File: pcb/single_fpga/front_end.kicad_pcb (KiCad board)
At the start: 4 copper layers, 120 x 120 mm, 71 parts, among them CON1 AXK680337YG, CON2 AXK680337YG, CON3 AXK680337YG, CON4 AXK680337YG, J1 Main Power Input, J2 AXK5S80337YG, J3 HR911130A, J4 JTAG_HDR_2x7_2mm, U1 TLV62569DBV, U3 DP83867IRRGZ, U4 TLV75525PDBV, U5 TLV75510PDRV, U6 TLV62569DBV, Y1 25MHz

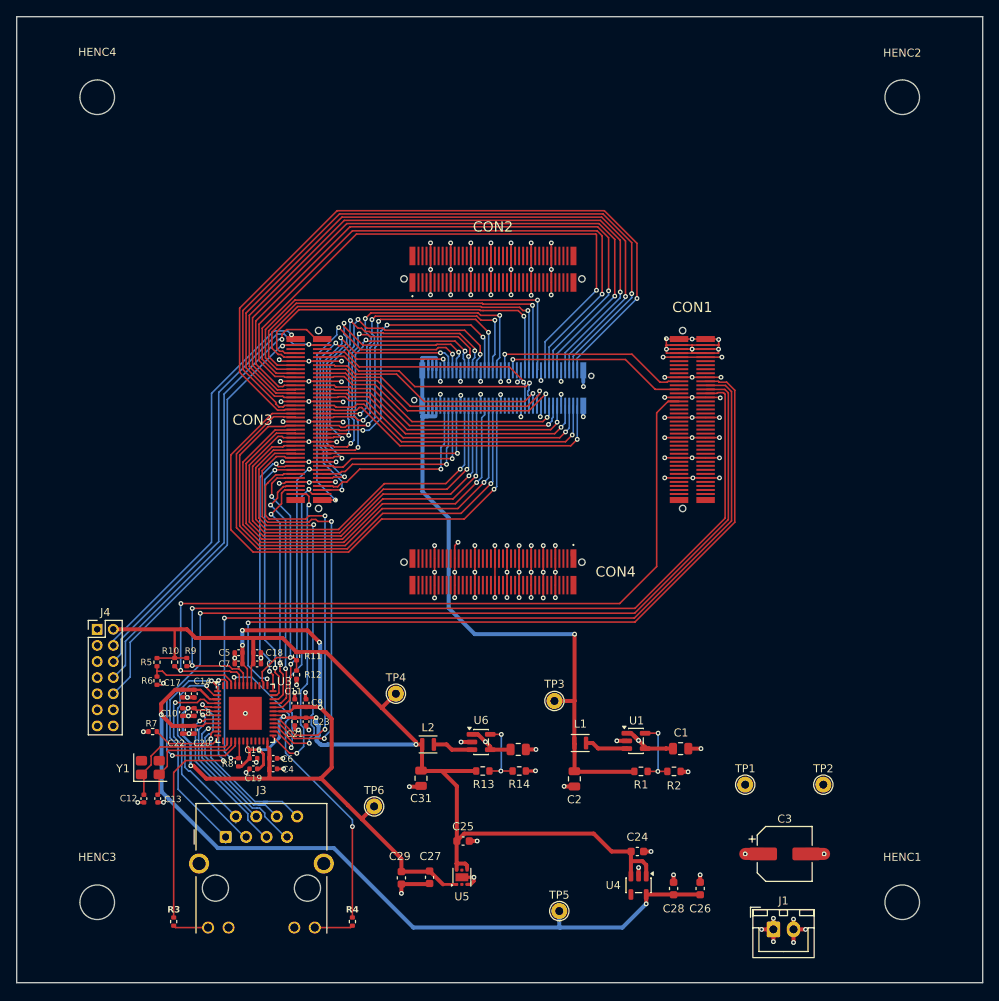
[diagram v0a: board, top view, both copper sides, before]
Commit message: Fixed thermal pad. Moved RGMII lines to be in the same bank.
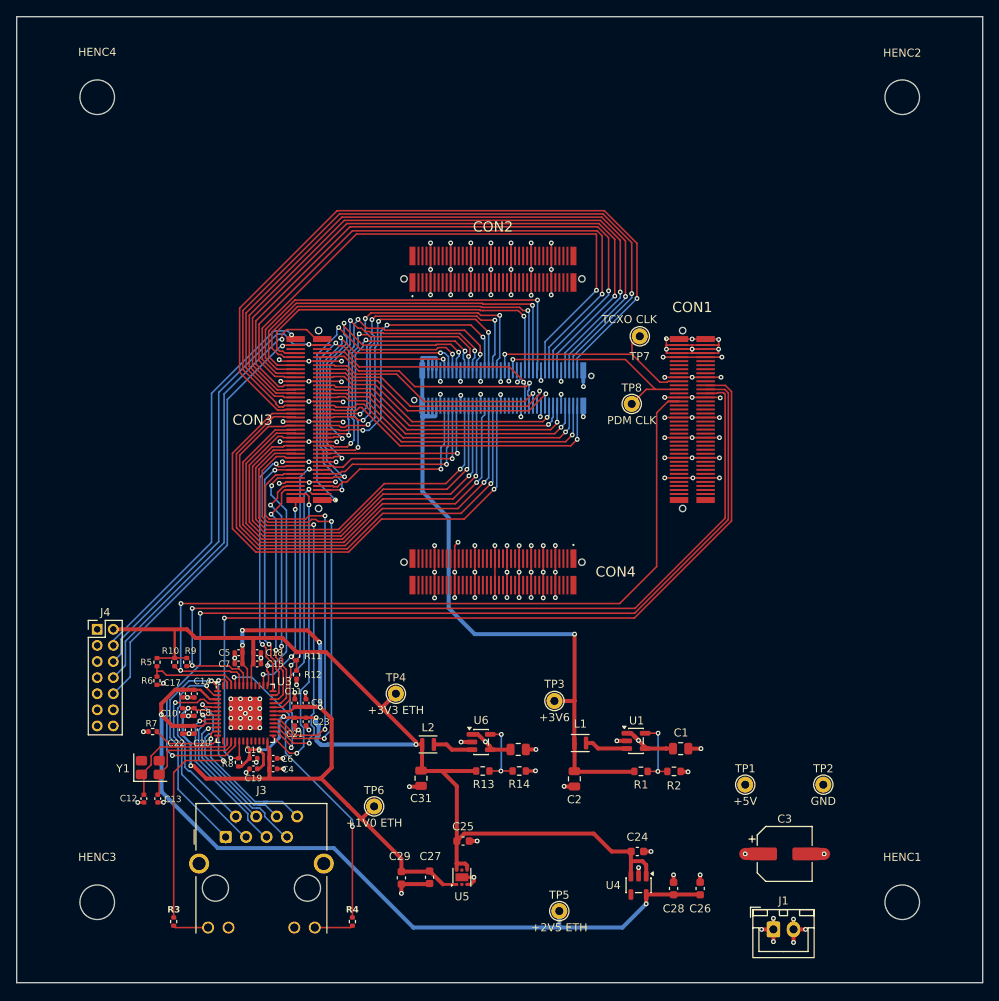
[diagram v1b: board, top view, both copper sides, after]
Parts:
- added TP7: TCXO CLK, TestPoint:TestPoint_THTPad_D2.0mm_Drill1.0mm, F.Cu at (117.4, 79.7)
- added TP8: PDM CLK, TestPoint:TestPoint_THTPad_D2.0mm_Drill1.0mm, F.Cu at (116.4, 88.1)
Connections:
- CON1 pad 22: RGMII_TX_CTL -> unconnected-(CON1-B13_L1_P-Pad22)
- CON3 pad 12: RGMII_RX_CTL -> RGMII_TX_CTL
- CON3 pad 2: unconnected-(CON3-B15_IO25-Pad2) -> RGMII_RX_CTL
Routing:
- net RGMII_TX_CTL: track 95.3 -> 30.7 mm
- net RGMII_RX_CTL: track 34.0 -> 27.7 mm, vias 2 -> 3
- net PDM_CLK: track 23.5 -> 27.2 mm
- net TCXO_CLK: track 25.1 -> 27.8 mm
- net GND: vias 143 -> 159

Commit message: Added more GND test points.
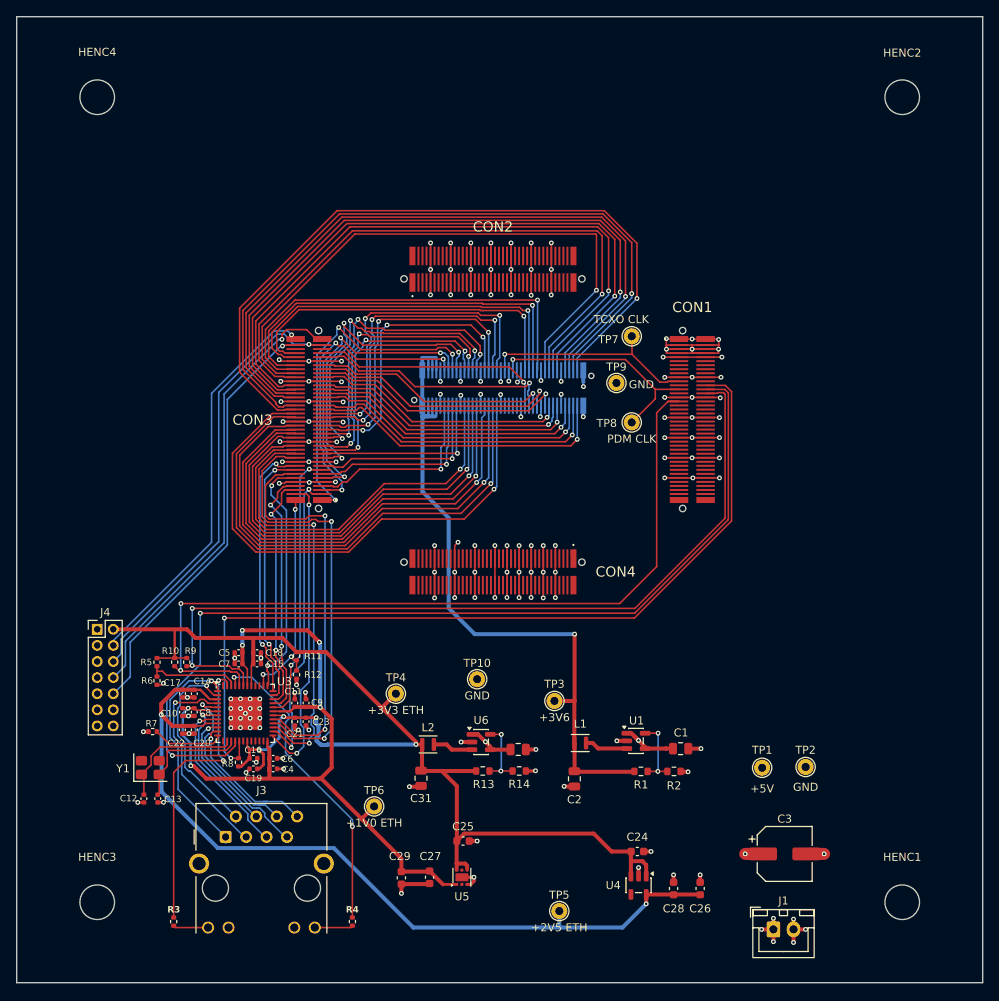
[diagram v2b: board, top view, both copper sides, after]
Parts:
- added TP10: GND, TestPoint:TestPoint_THTPad_D2.0mm_Drill1.0mm, F.Cu at (97.2, 122.3)
- added TP9: GND, TestPoint:TestPoint_THTPad_D2.0mm_Drill1.0mm, F.Cu at (114.5, 85.5)
- moved TP2 3.11 mm to (138.0, 133.2)
- moved TP1 2.97 mm to (132.6, 133.3)
- moved TP8 2.30 mm to (116.4, 90.4)
- moved TP7 1.00 mm to (116.4, 79.7)
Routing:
- net PDM_CLK: track 27.2 -> 28.8 mm

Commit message: Added RGB status LED.
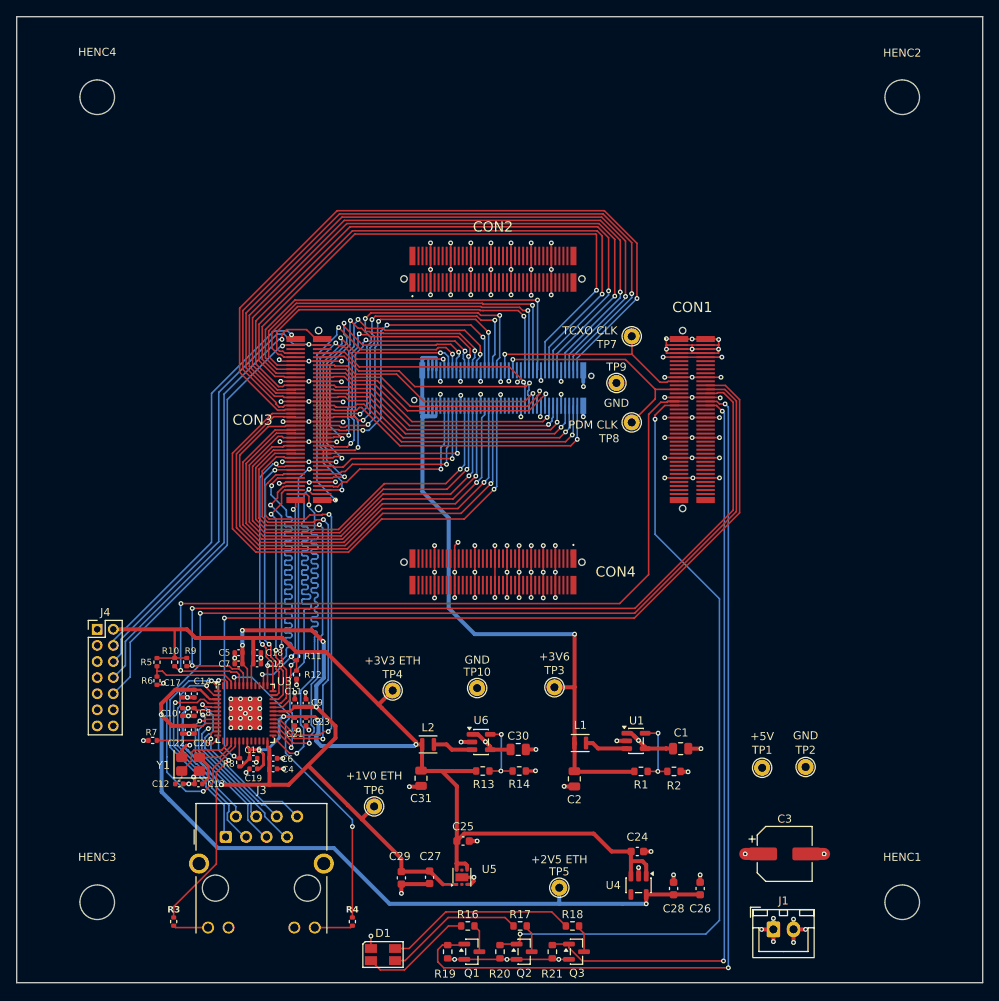
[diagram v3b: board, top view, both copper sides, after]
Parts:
- added D1: ASMB-MTB0-0A3A2, LED_SMD:LED_Avago_PLCC4_3.2x2.8mm_CW, F.Cu at (85.5, 156.5)
- added Q1: 2N7002, Package_TO_SOT_SMD:SOT-23, F.Cu at (96.5, 156.2)
- added Q2: 2N7002, Package_TO_SOT_SMD:SOT-23, F.Cu at (103.0, 156.2)
- added Q3: 2N7002, Package_TO_SOT_SMD:SOT-23, F.Cu at (109.5, 156.2)
- added R16: 620, PCM_SparkFun-Resistor:R_0603_1608Metric, F.Cu at (96.0, 152.9)
- added R17: 390, PCM_SparkFun-Resistor:R_0603_1608Metric, F.Cu at (102.5, 152.9)
- added R18: 390, PCM_SparkFun-Resistor:R_0603_1608Metric, F.Cu at (109.0, 152.9)
- added R19: 100k, PCM_SparkFun-Resistor:R_0603_1608Metric, F.Cu at (93.5, 156.2)
- added R20: 100k, PCM_SparkFun-Resistor:R_0603_1608Metric, F.Cu at (100.0, 156.2)
- added R21: 100k, PCM_SparkFun-Resistor:R_0603_1608Metric, F.Cu at (106.5, 156.2)
- Y1: value 25MHz -> 25MHz ±50 ppm max parallel resonant
- moved C13 5.38 mm to (62.6, 135.3), turned to 180 degrees
- moved Y1 5.02 mm to (61.6, 132.8)
- moved C12 4.74 mm to (60.2, 135.3), turned to 0 degrees
- moved TP5 2.90 mm to (107.4, 148.2)
- moved TP3 1.70 mm to (106.8, 123.3)
- moved TP10 1.10 mm to (97.2, 123.4)
- moved R7 1.10 mm to (56.9, 129.9)
- moved TP4 0.57 mm to (86.7, 123.7)
- moved R8 0.15 mm to (67.7, 132.6)
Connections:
- CON1 pad 32: unconnected-(CON1-B13_L6_P-Pad32) -> LED_R
- CON1 pad 33: unconnected-(CON1-B13_L3_N-Pad33) -> LED_G
- CON1 pad 34: unconnected-(CON1-B13_L6_N-Pad34) -> LED_B
- Y1 pad 2: Net-(U3-XI) -> GND
- Y1 pad 3: (no net) -> Net-(U3-XI)
- Y1 pad 4: (no net) -> GND
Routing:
- net LED_R: track 0.00 -> 114.3 mm, vias 0 -> 2
- net LED_G: track 0.00 -> 98.6 mm, vias 0 -> 2
- net LED_B: track 0.00 -> 93.3 mm, vias 0 -> 2
- net Net-(D1-BK): track 0.00 -> 23.8 mm
- net RGMII_TX_CTL: track 30.7 -> 50.7 mm
- net GND: track 274.4 -> 293.4 mm, vias 159 -> 163
- net Net-(D1-GK): track 0.00 -> 17.4 mm
- net Net-(D1-RK): track 0.00 -> 14.0 mm
- net RGMII_TXD2: track 38.6 -> 50.8 mm
- net RGMII_TXD3: track 38.6 -> 50.7 mm
- net MDC: track 117.6 -> 124.8 mm
- net Net-(U3-XO): track 15.9 -> 10.0 mm
- net Net-(U3-XI): track 14.6 -> 9.35 mm
- net Net-(Q3-D): track 0.00 -> 3.58 mm
- net Net-(Q2-D): track 0.00 -> 3.58 mm
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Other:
- board text added: "FAB NOTE: Vias in U3 (DP83867) exposed pad - 17 x 0.3 mm drill - epoxy filled and copper capped flat per IPC-4761 Type VII. All other vias: standard, tented both sides."

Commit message: Added status RGB LED. Moved RGMII signals to be in the same bank. Rerouted. DRC-/ERC-Clean.
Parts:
- moved C26 1.80 mm to (123.1, 148.3)
- moved C28 1.00 mm to (120.6, 148.3)
- moved C1 0.67 mm to (121.8, 130.9)
- moved TP3 0.51 mm to (107.3, 123.4)
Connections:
- CON3 pad 11: DATA_02 -> RGMII_RX_CTL
- CON3 pad 12: RGMII_TX_CTL -> RGMII_TXD0
- CON3 pad 13: DATA_03 -> RGMII_RXD2
- CON3 pad 16: RGMII_RXD2 -> RGMII_TX_CTL
- CON3 pad 17: DATA_05 -> RGMII_RXD3
- CON3 pad 18: RGMII_RXD3 -> DATA_05
- CON3 pad 2: RGMII_RX_CTL -> DATA_02
- CON3 pad 22: RGMII_TXD0 -> DATA_01
- CON3 pad 24: RGMII_TXD1 -> DATA_03
- CON3 pad 3: RGMII_TXD2 -> DATA_00
- CON3 pad 5: DATA_00 -> RGMII_RXD1
- CON3 pad 6: RGMII_RXD1 -> RGMII_TXD2
- CON3 pad 7: DATA_01 -> RGMII_RXD0
- CON3 pad 8: RGMII_RXD0 -> RGMII_TXD1
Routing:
- net DATA_03: track 23.3 -> 49.3 mm
- net DATA_05: track 23.2 -> 46.2 mm
- net DATA_01: track 23.8 -> 46.6 mm
- net RGMII_TX_CTL: track 50.7 -> 31.3 mm
- net RGMII_RXD3: track 32.6 -> 45.2 mm
- net RGMII_TXD2: track 50.8 -> 38.3 mm
- net RGMII_TXD3: track 50.7 -> 39.2 mm
- net RGMII_RX_CTL: track 28.1 -> 39.4 mm
- net RGMII_RXD2: track 32.6 -> 41.5 mm
- net RGMII_RXD1: track 29.6 -> 37.7 mm
- net RGMII_RXD0: track 31.2 -> 38.7 mm
- net DATA_02: track 38.6 -> 45.3 mm
- net RGMII_TXD1: track 53.0 -> 46.4 mm
- net +3V6: track 88.7 -> 92.5 mm
- net DATA_13: track 54.3 -> 57.6 mm
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
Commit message: Balanced RGMII lines.
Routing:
- net RGMII_TX_CTL: track 31.3 -> 50.1 mm
- net RGMII_TXD2: track 38.3 -> 50.2 mm
- net RGMII_TXD3: track 39.2 -> 50.1 mm
- net RGMII_RXC: track 33.9 -> 41.0 mm
- net RGMII_RXD3: track 45.2 -> 41.1 mm
- net RGMII_TXD1: track 46.4 -> 50.2 mm
- net RGMII_RX_CTL: track 39.4 -> 43.3 mm
- net RGMII_RXD1: track 37.7 -> 41.0 mm
- net RGMII_TXD0: track 53.6 -> 50.7 mm
- net RGMII_RXD0: track 38.7 -> 41.2 mm
- net RGMII_TXC: track 52.5 -> 50.4 mm
- net DATA_03: track 49.3 -> 47.6 mm
- net DATA_11: track 54.9 -> 53.2 mm
- net DATA_09: track 52.6 -> 50.9 mm
- net DATA_13: track 57.6 -> 56.0 mm
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
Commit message: Improved layout of regulators. Fixed capped/filled vias.
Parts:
- moved C1 10.2 mm to (111.6, 129.8), turned to -90 degrees
- moved C30 8.70 mm to (93.7, 129.7), turned to -90 degrees
- moved C26 7.50 mm to (115.6, 148.3)
- moved R2 5.13 mm to (119.4, 129.1)
- moved R14 4.70 mm to (101.9, 129.0)
- moved U4 4.45 mm to (112.8, 147.9)
- moved C24 4.45 mm to (112.7, 143.7)
- moved L2 3.91 mm to (93.9, 133.1), turned to -90 degrees
- moved TP5 3.80 mm to (103.6, 148.2)
- moved L1 3.47 mm to (111.7, 133.2), turned to -90 degrees
- moved R13 3.27 mm to (101.1, 133.0), turned to 90 degrees
- moved C28 3.10 mm to (117.5, 148.3)
- moved C29 2.54 mm to (90.3, 147.4)
- moved U1 2.28 mm to (115.3, 131.6)
- moved C27 1.40 mm to (92.6, 147.4)
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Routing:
- net GND: track 289.6 -> 312.4 mm, vias 161 -> 167
- net +3V3_ETH: track 152.9 -> 144.5 mm
- net LED_G: track 98.1 -> 90.9 mm
- net LED_R: track 113.4 -> 107.7 mm
- net +2V5_ETH: track 101.1 -> 95.6 mm
- net LED_B: track 92.9 -> 87.5 mm
- net Net-(U6-FB): track 8.85 -> 5.20 mm, vias 2 -> 0
- net Net-(U1-FB): track 8.87 -> 5.37 mm, vias 2 -> 0
- net Net-(U1-SW): track 5.35 -> 2.24 mm
- net +5V: track 53.2 -> 55.8 mm, vias 13 -> 15
- net +3V6: track 92.5 -> 94.9 mm
- net Net-(U6-SW): track 4.99 -> 2.66 mm
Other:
- board text added: "FAB NOTE: Vias in U3 (DP83867) and U5 (TLV75510) exposed pads - 19 x 0.3 mm drill (17 + 2) - epoxy filled and copper capped flat per IPC-4761 Type VII. All other vias: standard, tented both sides."
- board text removed: "FAB NOTE: Vias in U3 (DP83867) exposed pad - 17 x 0.3 mm drill - epoxy filled and copper capped flat per IPC-4761 Type VII. All other vias: standard, tented both sides."

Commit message: Added front silkscreen labels for power connector.
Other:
- board text added: "+5V"
- board text added: "GND"
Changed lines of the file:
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@@
 		(layer "Edge.Cuts")
+	)
+	(gr_text "+5V"
+		(at 129.9 159.5 0)
+		(layer "F.Cu")
+		(effects
+			(font
+				(size 1.5 1.5)
+				(thickness 0.3)
+				(bold yes)
+			)
+			(justify left bottom)
+		)
+	)
+	(gr_text "GND\n"
+		(at 135.9 159.5 0)
+		(layer "F.Cu")
+		(effects
+			(font
+				(size 1.5 1.5)
+				(thickness 0.3)
+				(bold yes)
+			)
+			(justify left bottom)
+		)
 	)
 	(gr_text "FAB NOTE: Vias in U3 (DP83867) and U5 (TLV75510) exposed pads - 19 x 0.3 mm drill (17 + 2) -\nepoxy filled and copper capped flat per IPC-4761 Type VII. All other vias: standard, tented both sides."

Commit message: Added more stitching caps and vias. Carved +5V island in In2.Cu and renamed.
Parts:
- added C32: 0.1uF, Capacitor_SMD:C_0402_1005Metric, F.Cu at (80.6, 145.7)
- added C33: 22uF, Capacitor_SMD:C_0805_2012Metric, F.Cu at (129.8, 83.4)
- added C34: 0.1uF, Capacitor_SMD:C_0402_1005Metric, F.Cu at (128.6, 80.9)
- moved C20 1.48 mm to (60.6, 128.6)
- moved C22 1.48 mm to (62.1, 128.6)
- moved C14 1.46 mm to (60.6, 124.1)
- moved C17 1.46 mm to (62.1, 124.1)
- moved C10 1.46 mm to (62.1, 126.4)
- moved C8 1.46 mm to (60.6, 126.4)
- moved C15 1.40 mm to (69.9, 119.0)
- moved C18 1.40 mm to (69.9, 120.4)
- moved C21 1.40 mm to (75.9, 127.6)
- moved C23 1.40 mm to (74.5, 127.6)
- moved C16 1.30 mm to (69.4, 133.4), turned to 180 degrees
- moved C19 1.30 mm to (69.4, 132.1), turned to 180 degrees
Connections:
- J3 pad 1: GND -> /Ethernet Interface/ETH_CT
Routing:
- net +5V: track 55.8 -> 87.3 mm, vias 15 -> 17
- net GND: track 312.4 -> 315.4 mm, vias 167 -> 196
- net /Ethernet Interface/ETH_CT: track 0.00 -> 2.46 mm
- added copper zone on In2.Cu, net GND
